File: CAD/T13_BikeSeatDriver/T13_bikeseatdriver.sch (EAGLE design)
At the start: 13 parts, among them U2 ATMEGA328P-PU

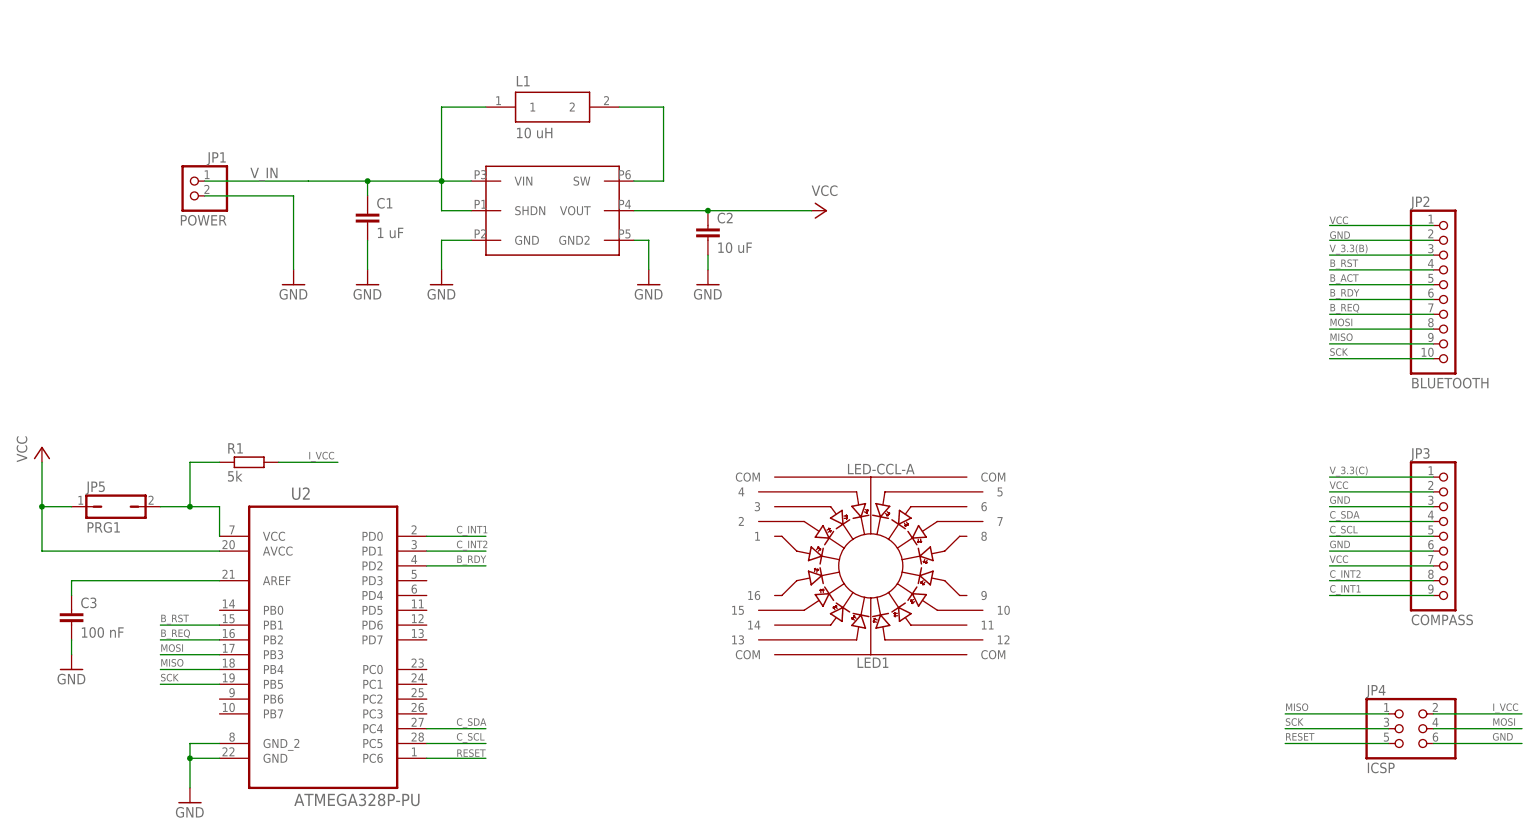
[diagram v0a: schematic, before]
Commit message: Add LED subsystem
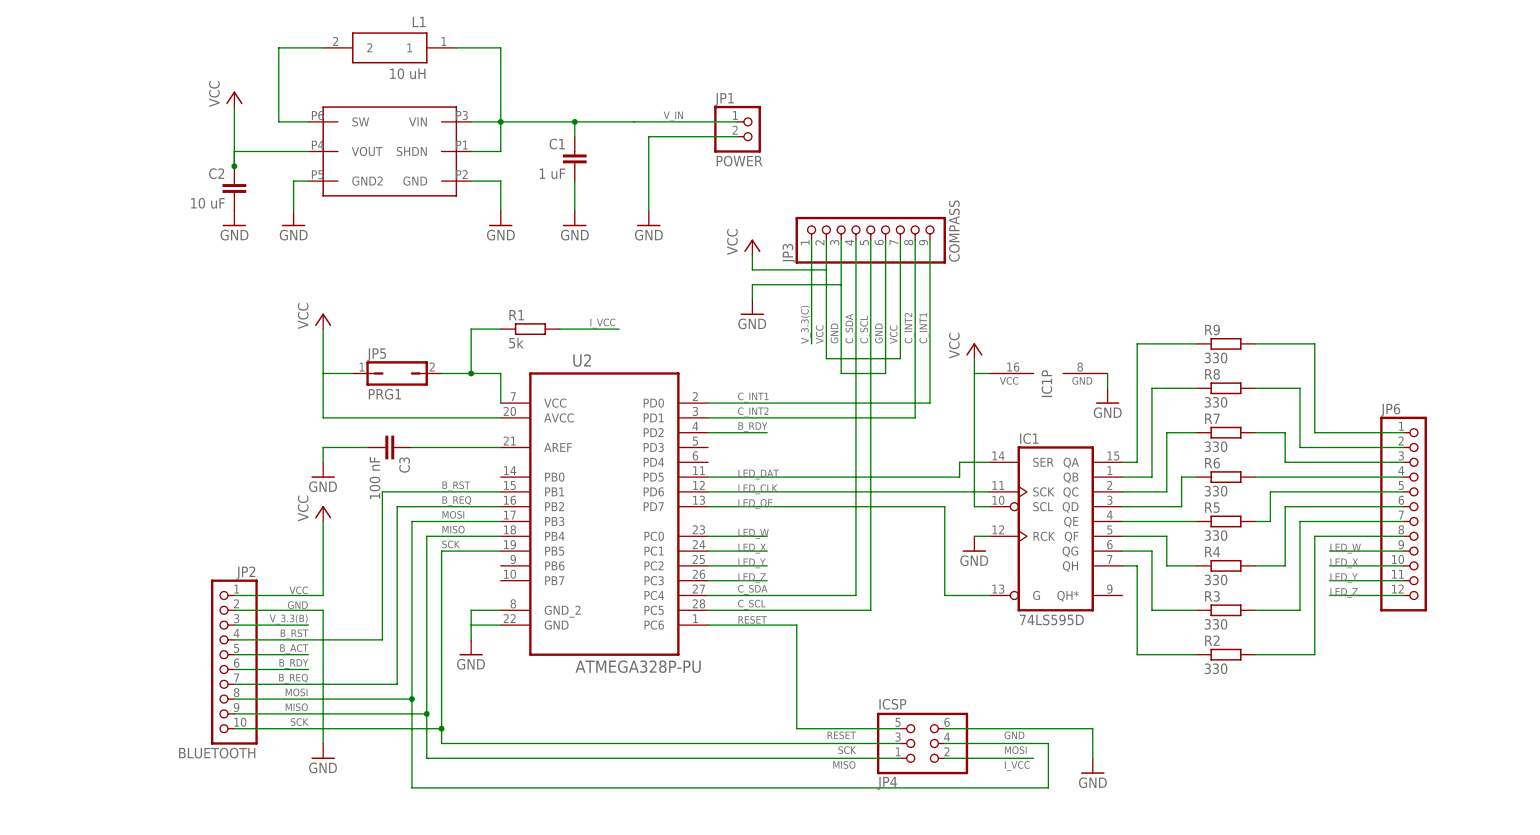
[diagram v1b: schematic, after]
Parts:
- removed LED1: LED-CCL-A, LED-CCL:LED-CCL-A
- added IC1: 74LS595D, 74xx-us:74LS595D
- added JP6: (no value), pinhead:PINHD-1X12
- added R2, R3, R4, R5, R6, R7, R8, R9: 330, eagle-ltspice:RR0603
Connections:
- new net LED_CLK: IC1A.SCK, U2.PD6
- new net LED_DAT: IC1A.SER, U2.PD5
- new net LED_OE: IC1A.G, U2.PD7
- new net LED_W: JP6.9, U2.PC0
- new net LED_X: JP6.10, U2.PC1
- new net LED_Y: JP6.11, U2.PC2
- new net LED_Z: JP6.12, U2.PC3
- new net N$10: IC1A.QB, R8.1
- new net N$11: IC1A.QA, R9.1
- new net N$12: JP6.1, R9.2
- new net N$13: JP6.2, R8.2
- new net N$14: JP6.3, R7.2
- new net N$15: JP6.4, R6.2
- new net N$16: JP6.5, R5.2
- new net N$17: JP6.6, R4.2
- new net N$18: JP6.7, R3.2
- new net N$19: JP6.8, R2.2
- new net N$4: IC1A.QH, R2.1
- new net N$5: IC1A.QG, R3.1
- new net N$6: IC1A.QF, R4.1
- new net N$7: IC1A.QE, R5.1
- new net N$8: IC1A.QD, R6.1
- new net N$9: IC1A.QC, R7.1
- net GND: now also IC1A.RCK, IC1P.GND
- net VCC: now also IC1A.SCL, IC1P.VCC
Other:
- moved on the sheet: C1, C2, C3, JP1, JP2, JP3, JP4, JP5, L1, R1, U2
